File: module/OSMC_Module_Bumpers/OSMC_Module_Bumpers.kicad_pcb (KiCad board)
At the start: 4 copper layers, 34 x 41 mm, 5 parts, among them SW1 SW_SPST, SW2 SW_SPST, U1 OSMC Module Board w/pins, U2 24LC02BT-I/OT, U3 PCF8574DWR

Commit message: reviewed PCBs
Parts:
- added JP1: SolderJumper_2_Bridged, Jumper:SolderJumper-2_P1.3mm_Bridged2Bar_Pad1.0x1.5mm, B.Cu at (186.6, 70.8)
- added JP2: SolderJumper_2_Bridged, Jumper:SolderJumper-2_P1.3mm_Bridged2Bar_Pad1.0x1.5mm, B.Cu at (188.3, 69.0)
- added JP3: SolderJumper_2_Bridged, Jumper:SolderJumper-2_P1.3mm_Bridged2Bar_Pad1.0x1.5mm, B.Cu at (190.2, 67.1)
- moved U2 22.2 mm to (188.0, 87.8)
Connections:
- U1 pad 18: unconnected-(U1-A3-Pad18) -> /A2
- U1 pad 19: unconnected-(U1-A2-Pad19) -> /A1
- U1 pad 20: unconnected-(U1-A1-Pad20) -> /A0
- U3 pad 1: GND -> /A0
- U3 pad 16: /5V -> /3v3
- U3 pad 2: GND -> /A1
- U3 pad 3: GND -> /A2
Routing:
- net /3v3: track 74.2 -> 7.87 mm, vias 0 -> 4
- net /A2: track 0.00 -> 32.2 mm, vias 0 -> 1
- net /A1: track 0.00 -> 32.1 mm, vias 0 -> 1
- net /A0: track 0.00 -> 31.2 mm, vias 0 -> 1
- net /SCL: track 57.8 -> 31.0 mm, vias 2 -> 1
- net /5V: track 52.9 -> 31.3 mm
- net /SDA: track 59.7 -> 38.9 mm, vias 2 -> 0
- net GND: track 31.2 -> 18.3 mm, vias 2 -> 6
- net unconnected-(U1-PadMP): track 11.2 -> 0.00 mm
- net /INT: track 48.6 -> 47.7 mm
- net /B1: track 16.1 -> 16.7 mm
- net /B2: track 18.9 -> 19.4 mm
- added copper zone on In2.Cu, net /3v3

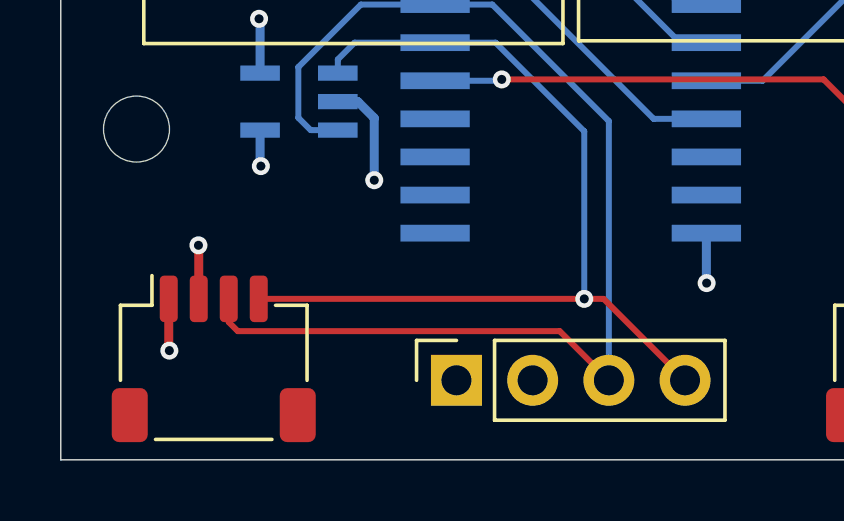
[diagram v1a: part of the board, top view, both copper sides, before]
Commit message: update to modules gerbers produced
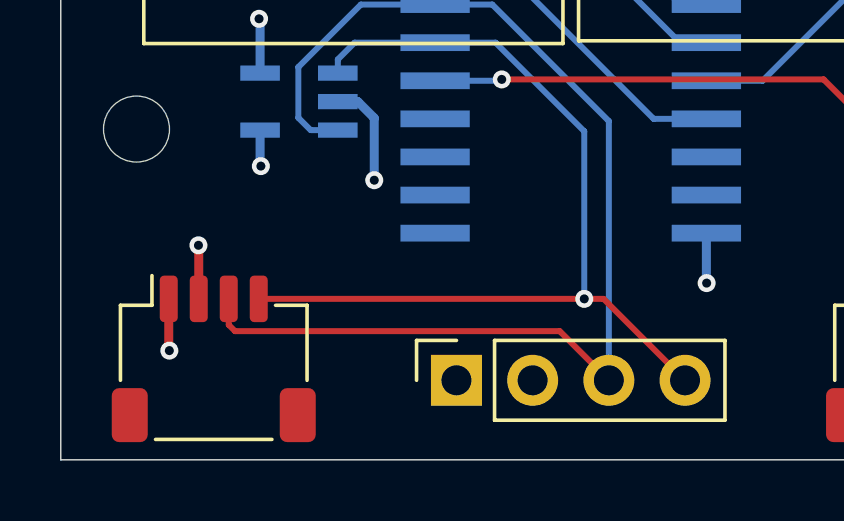
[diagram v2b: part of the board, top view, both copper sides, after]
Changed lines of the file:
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@@
 	)
 	(segment
-		(start 185.64 95.149999)
-		(end 185.64 94.375)
+		(start 185.851 95.451)
+		(end 185.64 95.24)
 		(width 0.2)
 		(layer "F.Cu")
@@
 	)
 	(segment
-		(start 185.941001 95.451)
-		(end 185.64 95.149999)
-		(width 0.2)
-		(layer "F.Cu")
-		(net 9)
-	)
-	(segment
-		(start 196.671 95.451)
-		(end 185.941001 95.451)
+		(start 185.64 95.24)
+		(end 185.64 94.375)
 		(width 0.2)
 		(layer "F.Cu")
@@
 		(width 0.2)
 		(layer "F.Cu")
+		(net 9)
+	)
+	(segment
+		(start 196.671 95.451)
+		(end 185.851 95.451)
+		(width 0.2)
+		(layer "F.Cu")

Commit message: created all gerber zips
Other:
- board text added: "BK MOD V1 2/26"
